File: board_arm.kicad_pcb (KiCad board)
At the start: 2 copper layers, 314.3 x 95.2 mm, 153 parts, among them SW1 SW_SPDT, U1 STM32F072CBT6, U2 PRTR5V0U2X, U3 MCP1725-3302E_SN

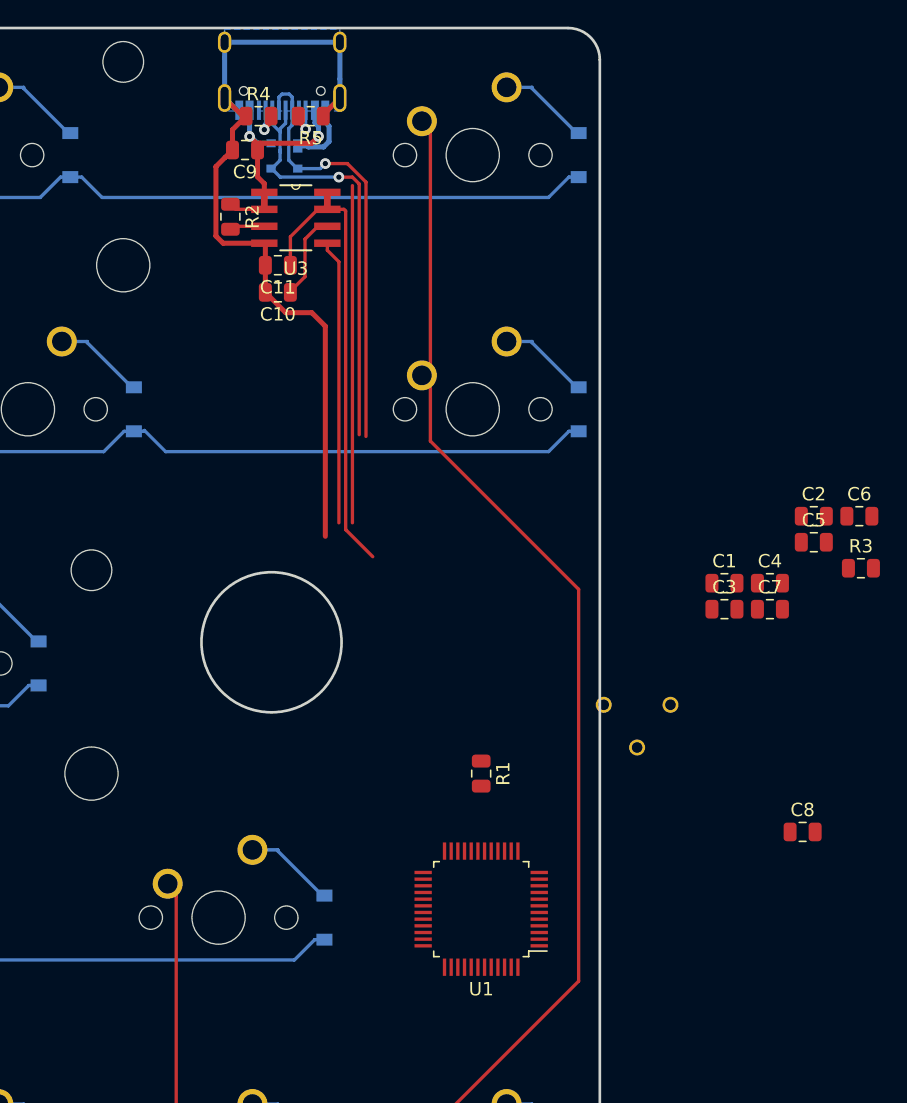
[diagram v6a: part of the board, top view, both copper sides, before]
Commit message: basic routing of sigs and power supply
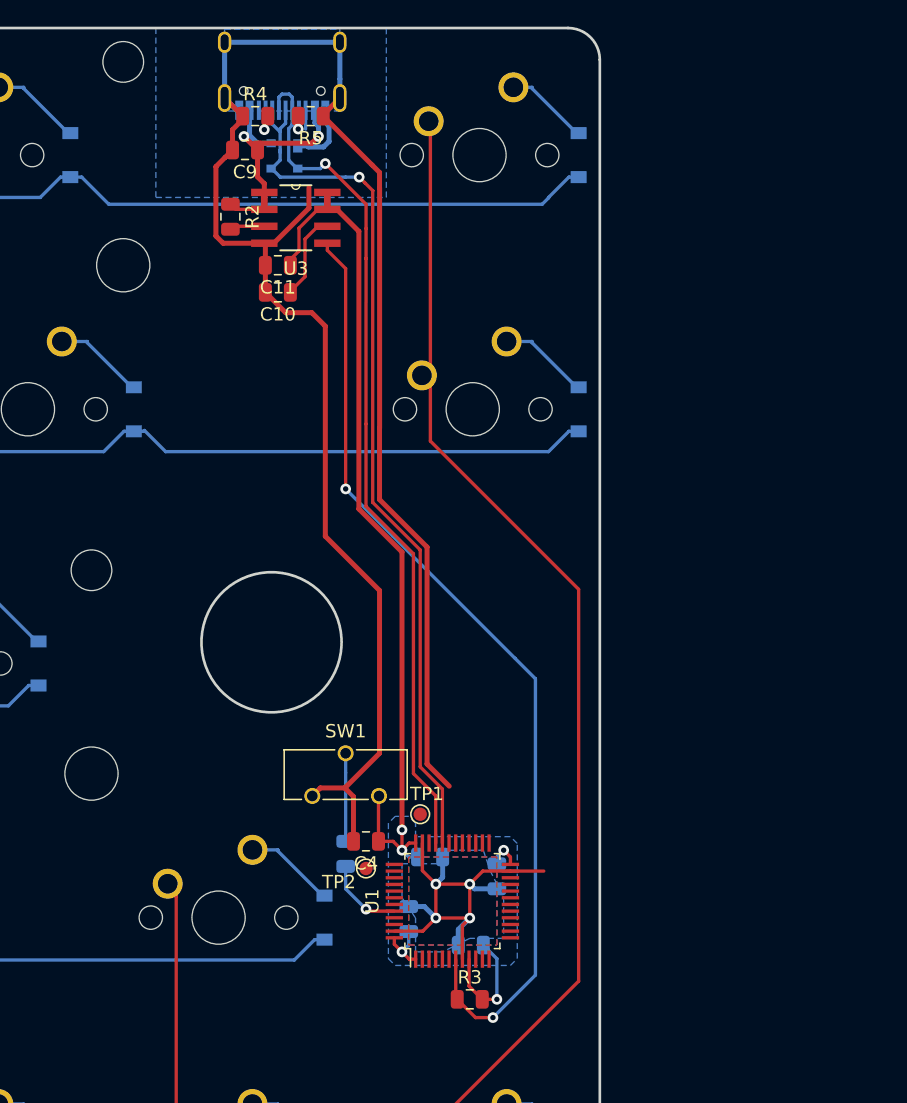
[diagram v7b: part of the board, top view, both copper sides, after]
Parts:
- removed C2, C3: 0.1uF, Capacitor_SMD:C_0805_2012Metric
- removed C5: 4.7uF, Capacitor_SMD:C_0805_2012Metric
- added TP1: TestPoint, TestPoint:TestPoint_Pad_D1.0mm, F.Cu at (348.5, 122.4)
- added TP2: TestPoint, TestPoint:TestPoint_Pad_D1.0mm, F.Cu at (344.4, 126.5)
- C1, C6, C7, C8, R1: moved to B.Cu
- SW1: moved to F.Cu
- moved R3 43.6 mm to (352.2, 136.3)
- moved C6 41.1 mm to (349.2, 125.6)
- moved C4 35.9 mm to (344.4, 124.5), turned to 180 degrees
- moved C7 33.7 mm to (352.3, 132.2), turned to 180 degrees
- moved C8 30.2 mm to (347.6, 130.3), turned to 90 degrees
- moved C1 27.8 mm to (354.2, 127.1), turned to 270 degrees
- moved SW1 22.1 mm to (342.9, 119.5)
- moved R1 11.8 mm to (342.9, 125.4), turned to 90 degrees
- moved U1 2.24 mm to (350.9, 128.9), turned to 90 degrees
- moved K_INSERT1 0.51 mm to (352.9, 73.0)
- moved R4 0.25 mm to (336.1, 70.1)
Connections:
- K_#1 pad 1: COL1 -> Net-(K_#1-Pad1)
- K_#10 pad 1: COL10 -> Net-(K_#10-Pad1)
- K_#2 pad 1: COL2 -> Net-(K_#2-Pad1)
- K_#3 pad 1: COL3 -> Net-(K_#3-Pad1)
- K_#4 pad 1: COL4 -> Net-(K_#4-Pad1)
- K_#5 pad 1: COL5 -> Net-(K_#5-Pad1)
- K_#6 pad 1: COL6 -> Net-(K_#6-Pad1)
- K_#7 pad 1: COL7 -> Net-(K_#7-Pad1)
- K_#8 pad 1: COL8 -> Net-(K_#8-Pad1)
- K_#9 pad 1: COL9 -> Net-(K_#9-Pad1)
- K_'1 pad 1: COL11 -> Net-(K_'1-Pad1)
- K_-1 pad 1: COL11 -> Net-(K_-1-Pad1)
- K_.1 pad 1: COL10 -> Net-(K_.1-Pad1)
- K_/1 pad 1: COL11 -> Net-(K_/1-Pad1)
- K_;1 pad 1: COL10 -> Net-(K_;1-Pad1)
- K_=1 pad 1: COL12 -> Net-(K_=1-Pad1)
- K_A1 pad 1: COL1 -> Net-(K_A1-Pad1)
- K_B1 pad 1: COL6 -> Net-(K_B1-Pad1)
- K_BACK1 pad 1: COL13 -> Net-(K_BACK1-Pad1)
- K_CAPS1 pad 1: COL0 -> Net-(K_CAPS1-Pad1)
- K_D1 pad 1: COL3 -> Net-(K_D1-Pad1)
- K_DELETE1 pad 1: COL15 -> Net-(K_DELETE1-Pad1)
- K_E1 pad 1: COL3 -> Net-(K_E1-Pad1)
- K_ENTER1 pad 1: COL13 -> Net-(K_ENTER1-Pad1)
- K_ESC1 pad 1: COL0 -> Net-(K_ESC1-Pad1)
- K_F1 pad 1: COL4 -> Net-(K_F1-Pad1)
- K_G1 pad 1: COL5 -> Net-(K_G1-Pad1)
- K_H1 pad 1: COL6 -> Net-(K_H1-Pad1)
- K_I1 pad 1: COL8 -> Net-(K_I1-Pad1)
- K_INSERT1 pad 1: COL15 -> Net-(K_INSERT1-Pad1)
- K_J1 pad 1: COL7 -> Net-(K_J1-Pad1)
- K_K1 pad 1: COL8 -> Net-(K_K1-Pad1)
- K_L1 pad 1: COL9 -> Net-(K_L1-Pad1)
- K_O1 pad 1: COL9 -> Net-(K_O1-Pad1)
- K_P1 pad 1: COL10 -> Net-(K_P1-Pad1)
- K_Q1 pad 1: COL1 -> Net-(K_Q1-Pad1)
- K_R1 pad 1: COL4 -> Net-(K_R1-Pad1)
- K_RSHIFT1 pad 1: COL12 -> Net-(K_RSHIFT1-Pad1)
- K_S1 pad 1: COL2 -> Net-(K_S1-Pad1)
- K_SHIFT1 pad 1: COL0 -> Net-(K_SHIFT1-Pad1)
- K_T1 pad 1: COL5 -> Net-(K_T1-Pad1)
- K_TAB1 pad 1: COL0 -> Net-(K_TAB1-Pad1)
- K_U1 pad 1: COL7 -> Net-(K_U1-Pad1)
- K_UP1 pad 1: COL14 -> Net-(K_UP1-Pad1)
- K_W1 pad 1: COL2 -> Net-(K_W1-Pad1)
- K_Y1 pad 1: COL6 -> Net-(K_Y1-Pad1)
- K_Z1 pad 1: COL2 -> Net-(K_Z1-Pad1)
- K_[1 pad 1: COL11 -> Net-(K_[1-Pad1)
- K_\1 pad 1: COL13 -> Net-(K_\1-Pad1)
- K_]1 pad 1: COL12 -> Net-(K_]1-Pad1)
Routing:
- net GND: track 93.1 -> 192.1 mm, vias 0 -> 4
- net PWRGD: track 21.3 -> 72.1 mm, vias 0 -> 2
- net +3V3: track 35.2 -> 81.7 mm, vias 0 -> 5
- net D-: track 32.7 -> 66.2 mm
- net D+: track 32.8 -> 64.5 mm
- net Net-(R1-Pad2): track 0.00 -> 6.60 mm
- net Net-(R1-Pad1): track 0.00 -> 6.02 mm, vias 0 -> 1
- net +5V: track 18.3 -> 19.0 mm
- added copper zone on B.Cu, net +3V3
- added copper zone on F.Cu, net GND

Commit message: corrections sur les TP
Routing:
- net SWDIO: track 0.00 -> 2.43 mm
- net SWDCLK: track 0.00 -> 2.25 mm
- net +3V3: track 81.7 -> 80.0 mm
- added copper zone on F.Cu, net +3V3
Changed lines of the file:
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@@
     (thickness 1.6)
     (drawings 9)
-    (tracks 1056)
+    (tracks 1058)
     (zones 0)
     (modules 152)
@@
     (42 Eco1.User user hide)
     (43 Eco2.User user hide)
-    (44 Edge.Cuts user hide)
+    (44 Edge.Cuts user)
     (45 Margin user hide)
     (46 B.CrtYd user hide)
@@
   (gr_arc (start 359.56875 156.36875) (end 359.56875 158.75) (angle -90) (layer Edge.Cuts) (width 0.2))
   (gr_arc (start 359.56875 65.88125) (end 361.95 65.88125) (angle -90) (layer Edge.Cuts) (width 0.2))
-  (via (at 344.424 129.54) (size 0.8) (drill 0.4) (layers F.Cu B.Cu) (net 101))
-  (via (at 354.234482 136.299484) (size 0.8) (drill 0.4) (layers F.Cu B.Cu) (net 98))
   (via (at 352.202482 130.203484) (size 0.8) (drill 0.4) (layers F.Cu B.Cu) (net 1))
   (via (at 349.662482 127.663484) (size 0.8) (drill 0.4) (layers F.Cu B.Cu) (net 1))
   (via (at 349.662482 130.203484) (size 0.8) (drill 0.4) (layers F.Cu B.Cu) (net 1))
-  (via (at 354.742482 125.123484) (size 0.8) (drill 0.4) (layers F.Cu B.Cu) (net 98))
-  (via (at 347.122482 125.123484) (size 0.8) (drill 0.4) (layers F.Cu B.Cu) (net 98))
-  (via (at 347.122482 132.743484) (size 0.8) (drill 0.4) (layers F.Cu B.Cu) (net 98))
   (via (at 352.202482 127.663484) (size 0.8) (drill 0.4) (layers F.Cu B.Cu) (net 1))
   (segment (start 334.7432 69.6618) (end 333.8282 68.7468) (width 0.375) (layer B.Cu) (net 1))
@@
   (segment (start 337.987001 72.644) (end 337.987001 71.287001) (width 0.25) (layer B.Cu) (net 92))
   (segment (start 337.362 74.036) (end 338.002 74.676) (width 0.25) (layer B.Cu) (net 92))
+  (segment (start 338.002 74.676) (end 342.9 74.676) (width 0.25) (layer B.Cu) (net 92))
+  (segment (start 342.9 74.676) (end 343.916 74.676) (width 0.25) (layer B.Cu) (net 92))
+  (segment (start 344.37052 75.13052) (end 344.92749 75.68749) (width 0.25) (layer F.Cu) (net 92))
+  (segment (start 343.916 74.676) (end 344.37052 75.13052) (width 0.25) (layer F.Cu) (net 92))
+  (segment (start 344.92749 75.68749) (end 344.932 75.692) (width 0.25) (layer F.Cu) (net 92))
+  (segment (start 344.92749 99.05549) (end 344.92749 75.68749) (width 0.25) (layer F.Cu) (net 92))
+  (segment (start 348.488 102.616) (end 344.92749 99.05549) (width 0.25) (layer F.Cu) (net 92))
+  (segment (start 348.488 118.872) (end 348.488 102.616) (width 0.25) (layer F.Cu) (net 92))
+  (segment (start 350.150482 124.587484) (end 350.150482 120.534482) (width 0.25) (layer F.Cu) (net 92))
+  (segment (start 350.150482 120.534482) (end 348.488 118.872) (width 0.25) (layer F.Cu) (net 92))
   (segment (start 336.8982 70.6368) (end 336.804 70.731) (width 0.25) (layer B.Cu) (net 93))
   (segment (start 336.8982 69.6618) (end 336.8982 70.6368) (width 0.25) (layer B.Cu) (net 93))
@@
   (segment (start 336.804 70.731) (end 336.804 70.731) (width 0.25) (layer B.Cu) (net 93))
   (via (at 336.804 71.12) (size 0.8) (drill 0.4) (layers F.Cu B.Cu) (net 93))
+  (segment (start 337.312 70.104) (end 337.312 70.612) (width 0.25) (layer F.Cu) (net 93))
+  (segment (start 336.804 70.3604) (end 337.0604 70.104) (width 0.25) (layer F.Cu) (net 93))
+  (segment (start 336.804 71.12) (end 336.804 70.3604) (width 0.25) (layer F.Cu) (net 93))
   (via (at 341.376 73.66) (size 0.8) (drill 0.4) (layers F.Cu B.Cu) (net 94))
   (segment (start 337.8982 68.6868) (end 338.132 68.453) (width 0.25) (layer B.Cu) (net 94))
@@
   (segment (start 339.262 74.036) (end 338.636999 73.410999) (width 0.25) (layer B.Cu) (net 94))
   (segment (start 339.312 74.036) (end 339.262 74.036) (width 0.25) (layer B.Cu) (net 94))
-  (segment (start 338.002 74.676) (end 342.9 74.676) (width 0.25) (layer B.Cu) (net 92))
-  (segment (start 342.9 74.676) (end 343.916 74.676) (width 0.25) (layer B.Cu) (net 92))
-  (segment (start 344.37052 75.13052) (end 344.92749 75.68749) (width 0.25) (layer F.Cu) (net 92))
-  (segment (start 343.916 74.676) (end 344.37052 75.13052) (width 0.25) (layer F.Cu) (net 92))
-  (segment (start 344.92749 75.68749) (end 344.932 75.692) (width 0.25) (layer F.Cu) (net 92))
-  (segment (start 344.92749 99.05549) (end 344.92749 75.68749) (width 0.25) (layer F.Cu) (net 92))
-  (segment (start 348.488 102.616) (end 344.92749 99.05549) (width 0.25) (layer F.Cu) (net 92))
-  (segment (start 348.488 118.872) (end 348.488 102.616) (width 0.25) (layer F.Cu) (net 92))
-  (segment (start 350.150482 124.587484) (end 350.150482 120.534482) (width 0.25) (layer F.Cu) (net 92))
-  (segment (start 350.150482 120.534482) (end 348.488 118.872) (width 0.25) (layer F.Cu) (net 92))
-  (segment (start 337.312 70.104) (end 337.312 70.612) (width 0.25) (layer F.Cu) (net 93))
-  (segment (start 336.804 70.3604) (end 337.0604 70.104) (width 0.25) (layer F.Cu) (net 93))
-  (segment (start 336.804 71.12) (end 336.804 70.3604) (width 0.25) (layer F.Cu) (net 93))
   (segment (start 341 74.036) (end 341.376 73.66) (width 0.25) (layer B.Cu) (net 94))
   (segment (start 339.312 74.036) (end 341 74.036) (width 0.25) (layer B.Cu) (net 94))
@@
   (segment (start 339.344 70.104) (end 339.344 70.5196) (width 0.25) (layer F.Cu) (net 95))
   (segment (start 339.344 70.104) (end 339.344 71.0738) (width 0.25) (layer F.Cu) (net 95))
+  (via (at 354.234482 136.299484) (size 0.8) (drill 0.4) (layers F.Cu B.Cu) (net 98))
+  (via (at 354.742482 125.123484) (size 0.8) (drill 0.4) (layers F.Cu B.Cu) (net 98))
+  (via (at 347.122482 125.123484) (size 0.8) (drill 0.4) (layers F.Cu B.Cu) (net 98))
+  (via (at 347.122482 132.743484) (size 0.8) (drill 0.4) (layers F.Cu B.Cu) (net 98))
   (segment (start 341.5284 77.089) (end 341.5284 75.819) (width 0.508) (layer F.Cu) (net 98))
   (segment (start 340.8172 77.089) (end 341.5284 77.089) (width 0.25) (layer F.Cu) (net 98))
@@
   (segment (start 342.2396 77.089) (end 341.5284 77.089) (width 0.375) (layer F.Cu) (net 98))
   (segment (start 343.8906 78.74) (end 342.2396 77.089) (width 0.375) (layer F.Cu) (net 98))
-  (segment (start 346.458998 124.46) (end 347.122482 125.123484) (width 0.25) (layer F.Cu) (net 98))
   (segment (start 345.3615 124.46) (end 346.458998 124.46) (width 0.25) (layer F.Cu) (net 98))
   (segment (start 347.122482 125.123484) (end 347.122482 123.599484) (width 0.25) (layer F.Cu) (net 98))
-  (segment (start 347.658482 124.587484) (end 347.122482 125.123484) (width 0.25) (layer F.Cu) (net 98))
   (segment (start 348.150482 124.587484) (end 347.658482 124.587484) (width 0.25) (layer F.Cu) (net 98))
   (segment (start 343.8906 78.74) (end 343.8906 99.5426) (width 0.375) (layer F.Cu) (net 98))
@@
   (segment (start 339.852 79.3242) (end 340.8172 78.359) (width 0.25) (layer F.Cu) (net 100))
   (segment (start 339.852 82.139) (end 339.852 79.3242) (width 0.25) (layer F.Cu) (net 100))
+  (via (at 344.424 129.54) (size 0.8) (drill 0.4) (layers F.Cu B.Cu) (net 101))
   (segment (start 344.571484 129.687484) (end 344.424 129.54) (width 0.25) (layer F.Cu) (net 101))
   (segment (start 346.550482 129.687484) (end 344.571484 129.687484) (width 0.25) (layer F.Cu) (net 101))
   (segment (start 342.9 128.016) (end 344.424 129.54) (width 0.25) (layer B.Cu) (net 101))
   (segment (start 342.9 126.335) (end 342.9 128.016) (width 0.25) (layer B.Cu) (net 101))
+  (segment (start 349.150482 123.090482) (end 348.488 122.428) (width 0.25) (layer F.Cu) (net 127))
+  (segment (start 349.150482 124.587484) (end 349.150482 123.090482) (width 0.25) (layer F.Cu) (net 127))
+  (segment (start 344.728516 126.187484) (end 344.424 126.492) (width 0.25) (layer F.Cu) (net 128))
+  (segment (start 346.550482 126.187484) (end 344.728516 126.187484) (width 0.25) (layer F.Cu) (net 128))
   (zone (net 1) (net_name GND) (layer B.Cu) (hatch edge 0.508)
     (connect_pads (clearance 0.381))
@@
       )
     )
+  )
+  (zone (net 98) (net_name +3V3) (layer F.Cu) (hatch edge 0.508)
+    (connect_pads (clearance 0.381))
+    (min_thickness 0.254)
+    (fill yes (arc_segments 16) (thermal_gap 0.508) (thermal_bridge_width 0.508))
+    (polygon
+      (pts
+        (xy 345.44 120.904) (xy 346.964 119.38) (xy 348.488 120.904) (xy 348.488 125.476) (xy 345.948 125.476)
+        (xy 345.44 124.968)
+      )
+    )
